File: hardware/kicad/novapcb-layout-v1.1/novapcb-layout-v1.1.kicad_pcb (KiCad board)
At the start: 6 copper layers, 90 x 70 mm, 129 parts, among them J1 USB-C_2.0, J10 CRSF_solder_pad, J11 ESC_solder_pad, J12 ESC_solder_pad, J13 ESC_solder_pad, J14 ESC_solder_pad, J15 ESC_solder_pad, J16 ESC_solder_pad, J17 ESC_solder_pad, J18 ESC_solder_pad, J19 MAUCH2_6P, J2 microSD_DM3AT, J20 CAN_4P, J3 TELEM_6P, J4 MAUCH_6P, J5 GPS_MAG_10P, J9 SWD_10P, Q2 AO3401A, Q3 AO4262E, Q4 AO4262E, Q5 AO3400A, U1 STM32H743VITx, U11 LM74700-Q1, U12 LM74700-Q1, U13 LP5907MFX-3.3, U14 TJA1051TK/3, U15 PESD2CAN, U2 AP2112K-3.3, U3 ICM-42688-P_LGA-14_2.5x3mm_P0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, U4 DPS310, U5 USBLC6-2P6, U6 TPS25940A, U7 LPS22HB, U8 BMI088, U9 LSM6DSV16X, Y1 8MHz

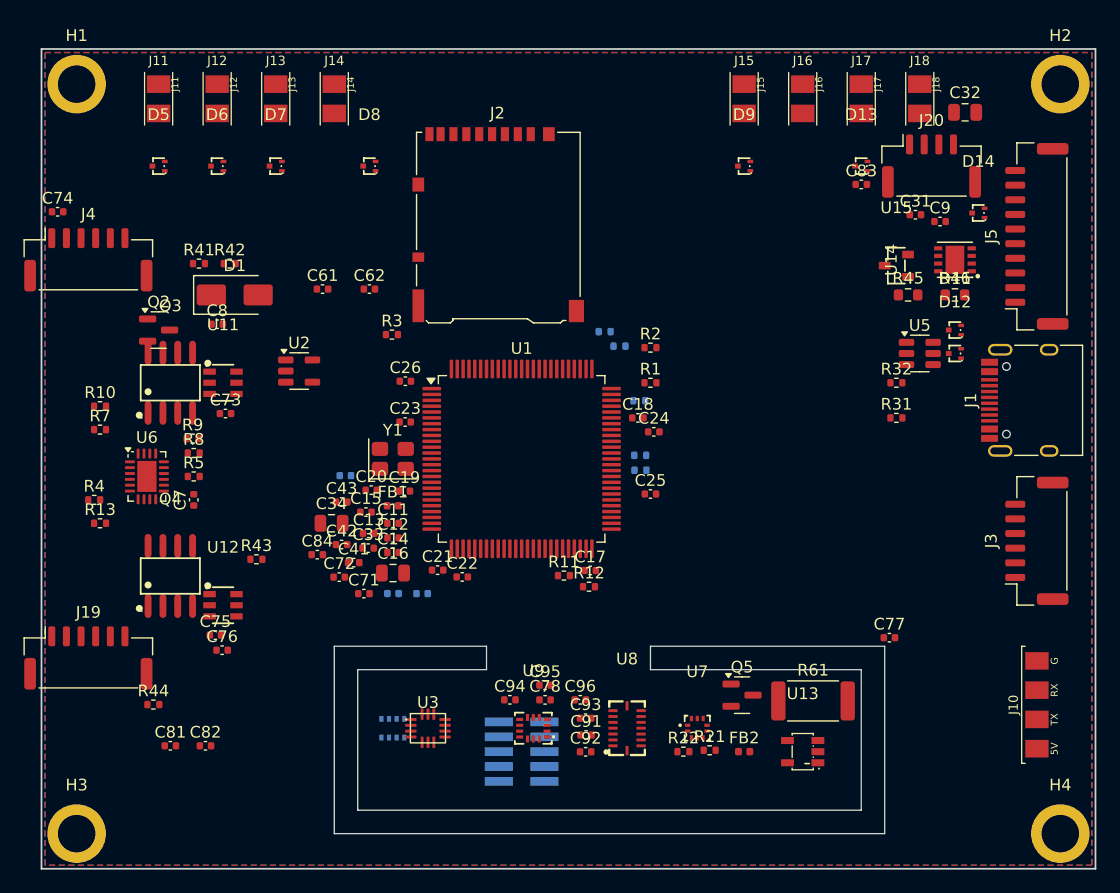
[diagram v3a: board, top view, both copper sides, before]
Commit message: hw: R4 Freerouting on valid re-mux v13 — plateau at 37 unrouted (77% routed)
Master's gate: ~100% completion required. Result: 77% (plateau at
36-37 unrouted across passes 11-21). BELOW gate; below master's
quoted ~85% original-placement plateau.

Freerouting v2.2.3 -mp 30, 33 min, 21 passes:
  pass  1: 82 unrouted
  pass  6: 44
  pass 10: 40
  pass 11: 36  (lowest)
  pass 21: 37  (final — plateau)

PCB state after SES import: 610 tracks + 54 vias placed.
DRC: 144 unconnected items (was 235 before routing) — 91 connections
made. Net topology: 37 of 159 nets fully unrouted.

Compare to ORIGINAL placement -mp 30: 25 unrouted (84% routed).
The re-placement actually performed WORSE — 12 more nets unrouted.

Likely reasons (honest):
1. Sensor island on S edge forces SPI3 (PB3/4/5 on N) + I2C1 (PB6/7
   on N) to traverse the entire board diagonally. ~6 long traces from
   MCU-N down to S-island = the routing bottleneck.
2. ESC pads on N edge force MOT3/MOT4 (PA0/PA1 on W) + MOT7/MOT8
   (PD12/PD13 on E) to route across the board to N-edge ESC pads.
3. The LQFP-100 pin-mux locked SPI3/I2C1 to N, which conflicts with
   sensor-island-on-S strategy. Master's strategy assumed re-mux
   could fix this; it cannot on this package.

Per master's authorized fallback: stackup layer-rebalance — convert
inner plane layer(s) to signal layers for routing room.

Renders: render_fr_v13_top.png + bot.png

Co-Authored-By: Claude Opus 4.7 <noreply@anthropic.com>
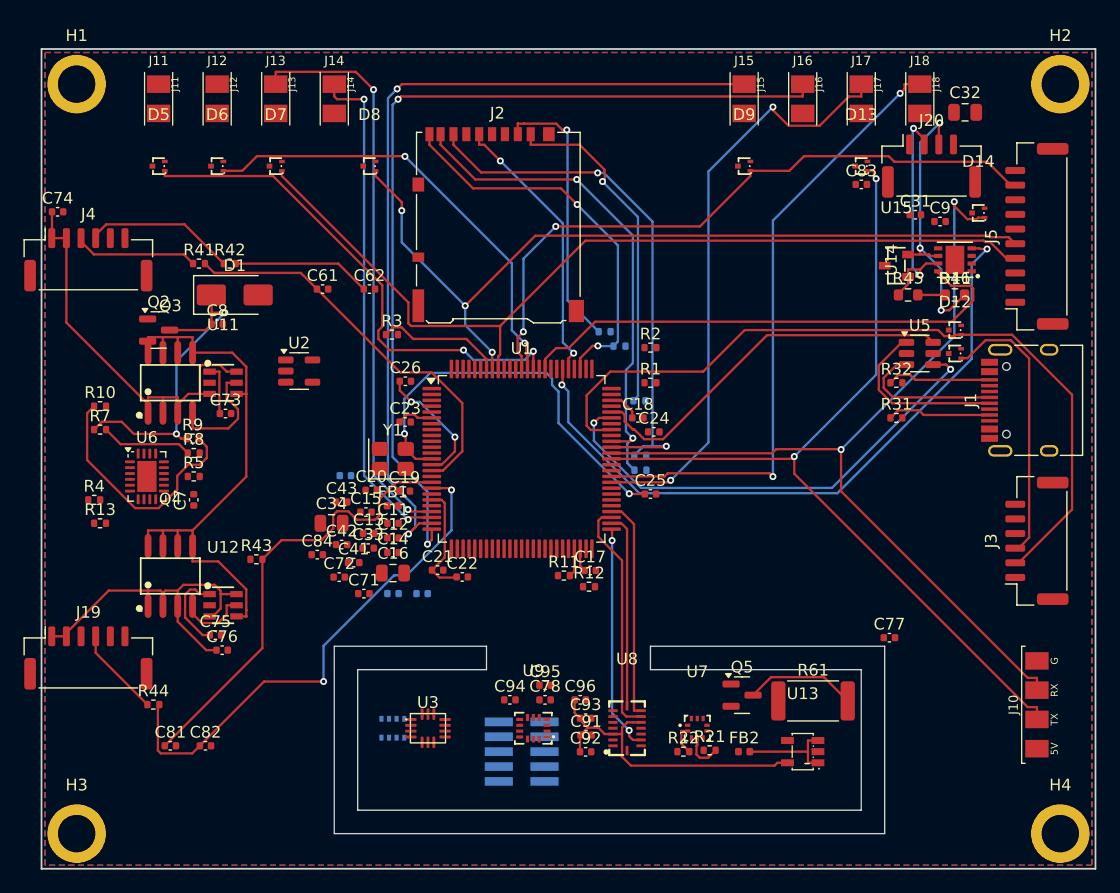
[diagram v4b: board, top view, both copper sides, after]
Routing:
- net I2C1_SCL: track 0.00 -> 79.4 mm
- net MOT6: track 0.00 -> 76.6 mm, vias 0 -> 2
- net USART6_RX: track 0.00 -> 76.4 mm, vias 0 -> 2
- net USART6_TX: track 0.00 -> 75.1 mm, vias 0 -> 2
- net I2C1_SDA: track 0.00 -> 74.2 mm, vias 0 -> 3
- net MOT5: track 0.00 -> 71.7 mm, vias 0 -> 2
- net USART1_TX: track 0.00 -> 67.6 mm
- net CAN1_RX: track 0.00 -> 57.8 mm, vias 0 -> 2
- net BUZZER: track 0.00 -> 56.7 mm, vias 0 -> 2
- net MOT8: track 0.00 -> 53.5 mm, vias 0 -> 2
- net MOT7: track 0.00 -> 51.1 mm, vias 0 -> 2
- net +5V_BEC: track 0.00 -> 51.0 mm
- net MOT3: track 0.00 -> 49.2 mm, vias 0 -> 2
- net SDMMC1_D0: track 0.00 -> 47.6 mm, vias 0 -> 2
- net GPIO_CAN1_SILENT: track 0.00 -> 44.2 mm
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
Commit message: hw: R4 stackup layer-rebalance — L4 becomes signal (master 2026-05-22)
Master's authorized fallback after re-placement plateau (77% < gate).

Stackup change (KEEP same 6-layer JLC06161H-7628 fab — only L4 copper
role changes):
  OLD: L1 Sig / L2 GND / L3 +3V3 / L4 +5V / L5 GND / L6 Sig (2 sig)
  NEW: L1 Sig / L2 GND / L3 +3V3 / L4 SIGNAL / L5 GND / L6 Sig (3 sig)

+50% routing room. Every signal layer adjacent to a reference plane
(L1→L2, L4→L3/L5, L6→L5). No adjacent-signal crosstalk.

Applied:
- layer_rebalance.py: removed 2 +5V zones from In3.Cu, stripped routes
- USB pair impedance recompute on new stackup (IMPEDANCE_RECOMPUTE_L4.md):
  - L1 + L6: W=0.30/S=0.10 (unchanged) → Z_diff = 94.4Ω ✓
  - L4: W=0.16/S=0.10 → Z_diff ≈ 87Ω ✓ (within USB ±15%)
  - Decision: USB pair stays L1/L6 to avoid via geometry discontinuity;
    L4 for all OTHER signals (~150 nets, the bottleneck)
- run_3layer.py: Freerouting now keeps In3.Cu as signal layer, strips
  In1/In2/In4 + plane nets (only GND + +3V3 remain as planes; +5V is
  now a routed signal).

PCB unchanged geometrically: placement v13, slot, smalls — all kept.
ONLY L4's copper role changes.

Freerouting v2.2.3 -mp 30 running on 3-signal stackup.

Co-Authored-By: Claude Opus 4.7 <noreply@anthropic.com>
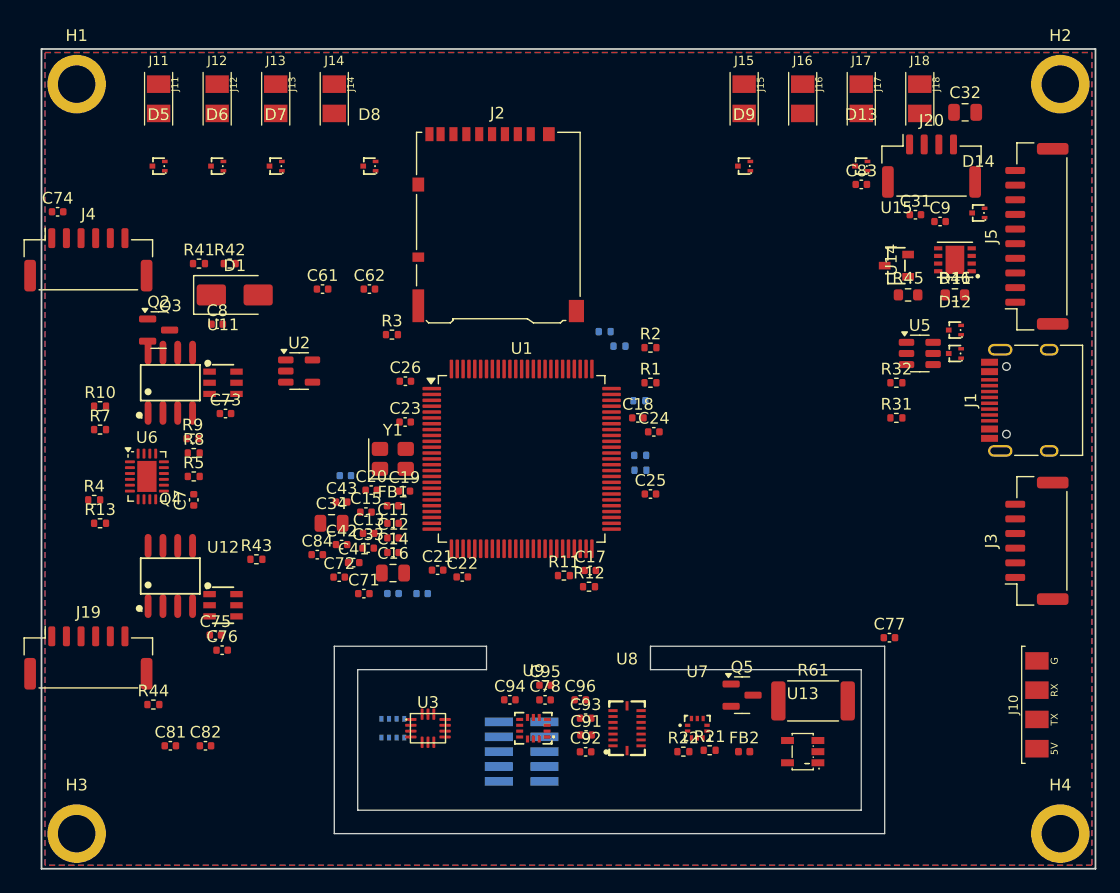
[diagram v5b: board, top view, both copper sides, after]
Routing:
- net I2C1_SCL: track 79.4 -> 0.00 mm
- net MOT6: track 76.6 -> 0.00 mm, vias 2 -> 0
- net USART6_RX: track 76.4 -> 0.00 mm, vias 2 -> 0
- net USART6_TX: track 75.1 -> 0.00 mm, vias 2 -> 0
- net I2C1_SDA: track 74.2 -> 0.00 mm, vias 3 -> 0
- net MOT5: track 71.7 -> 0.00 mm, vias 2 -> 0
- net USART1_TX: track 67.6 -> 0.00 mm
- net CAN1_RX: track 57.8 -> 0.00 mm, vias 2 -> 0
- net BUZZER: track 56.7 -> 0.00 mm, vias 2 -> 0
- net MOT8: track 53.5 -> 0.00 mm, vias 2 -> 0
- net MOT7: track 51.1 -> 0.00 mm, vias 2 -> 0
- net +5V_BEC: track 51.0 -> 0.00 mm
- net MOT3: track 49.2 -> 0.00 mm, vias 2 -> 0
- net SDMMC1_D0: track 47.6 -> 0.00 mm, vias 2 -> 0
- net GPIO_CAN1_SILENT: track 44.2 -> 0.00 mm
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- removed copper zone on In3.Cu, net +5V

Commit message: hw: R4 3-layer Freerouting — 88.8% routed (20 unrouted), SES applied
3-signal stackup (L1/L4/L6) + v13 placement + valid re-mux:
- Java FR completed naturally at -mp 30 in 2h 2min (pass 26 plateau)
- 179 nets total → 20 unrouted → 159 routed = **88.8%**
- Improved from 2-signal result: 25 (84%) → 20 (88.8%) = +4.8 pts
- SES on disk (76 KB), imported successfully

Process note: pre-empted my Python wrapper's 2h TIMEOUT by SIGKILL'ing
the wrapper (PID 1685284) at 53min mark, orphaning Java FR (1685298)
to init. Java continued unimpeded, completed naturally, wrote SES.
Master's reinforced lesson applied: timeouts are safety nets, never
guillotines on converging runs.

PCB state: 988 tracks + 113 vias
DRC: 0 shorts, 3 minor copper_edge_clearance (0.21-0.23mm vs 0.30
required); 112 unconnected items (= 20 unrouted nets)

Unrouted residual (15 net names):
  BATT_CURRENT_SENS, GND (one segment), IMU3_CS, IMU3_INT1, MOT1,
  MOT2, NRST, SPI1_MISO/MOSI/SCK, SPI3_MISO/MOSI/SCK, SWCLK, SWDIO

Most are island↔MCU long traces (SPI1, SPI3, IMU3) confirming the
LQFP-100 pin-mux constraint flagged earlier.

+5V WIDTH ISSUE: all 108 +5V track segments are 0.20mm (Default
netclass). Per master's 3A spec, +5V needs ≥1.5-1.8mm trace OR pour
on signal layer. Pending fix.

Per master's directive on meaningful residual: STOP for master's
call. Options: 4-signal fallback (convert L3 too), finishing pass
on the 15 residual nets, or accept and route 15 manually.

Co-Authored-By: Claude Opus 4.7 <noreply@anthropic.com>
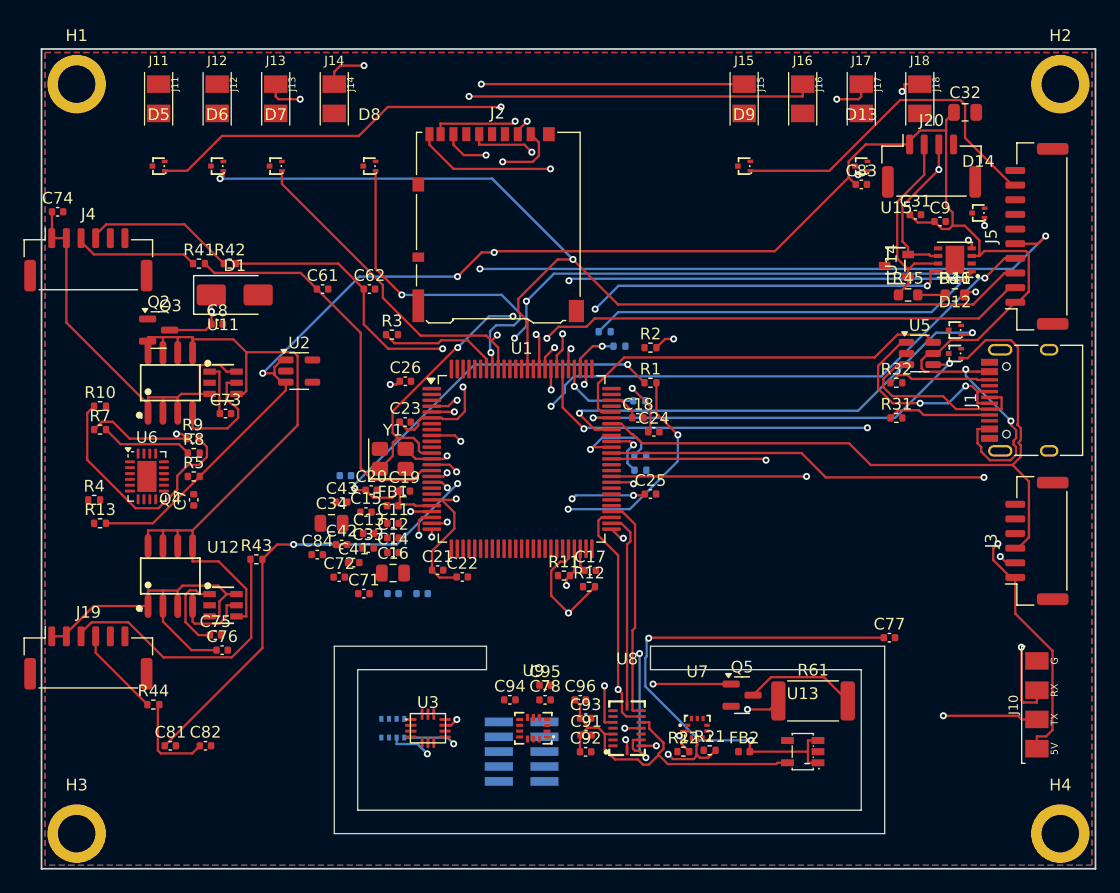
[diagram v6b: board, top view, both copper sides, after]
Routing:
- net +5V: track 0.00 -> 243.0 mm, vias 0 -> 7
- net I2C1_SDA: track 0.00 -> 135.8 mm, vias 0 -> 5
- net I2C1_SCL: track 0.00 -> 117.9 mm, vias 0 -> 4
- net SDMMC1_CMD: track 0.00 -> 99.2 mm, vias 0 -> 4
- net GPS1_TX: track 0.00 -> 94.1 mm, vias 0 -> 2
- net GPS1_RX: track 0.00 -> 86.7 mm, vias 0 -> 2
- net USART6_RX: track 0.00 -> 84.9 mm, vias 0 -> 3
- net USART6_TX: track 0.00 -> 78.6 mm, vias 0 -> 3
- net IMU2_GYR_CS: track 0.00 -> 76.7 mm, vias 0 -> 2
- net MOT6: track 0.00 -> 69.3 mm, vias 0 -> 2
- net VBAT: track 0.00 -> 64.5 mm, vias 0 -> 2
- net MOT5: track 0.00 -> 63.3 mm, vias 0 -> 2
- net USART1_TX: track 0.00 -> 62.4 mm, vias 0 -> 3
- net +5V_BEC: track 0.00 -> 61.7 mm
- net USART1_RX: track 0.00 -> 60.4 mm
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
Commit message: hw: R4 plane-stitch on clean FR3 baseline — 67→30 unconnected
Per master 2026-05-22: do plane stitches NOW on clean FR3 baseline
(commit 14a2d46) — mechanical, headless-doable, needed regardless of
the 12 signal residuals.

Step 1: run_stitch_plane_nets.py
- 176 pads stitched ✓ (vs 170 on tangled board — clean is better)
- 8 skipped (TH) + 1 already-via
- 15 failed (dense MCU/USB areas)

Step 2: fix_mcu_power.py (MCU power pin → decap trace approach)
- 8 GND traces added: U12.2, U9.6, U8.4/6/7, U1.10/19/26 → nearest decap

Net effect: unconnected 67 → 30, DRC 0 → 59 (clashes introduced by stitches+traces)

Remaining 30 unconnected breakdown:
- 12 signal residuals (HELD per master directive — untouched)
- 18 plane items still need stitching/connection:
  - +3V3_IMU: 9 items (C78/C94/C95, U9.5/8) — NOT plane-stitch; needs
    routing from FB2 ferrite output to consumers (separate net)
  - +3V3: 6 items (U1.11/50/75 power pins + a few others — dense MCU
    region where stitch+decap-trace both failed)
  - GND: U1.74, U1.50 (dense MCU power pins)
  - Plus pads on signal-net residuals (U1.86=GPS1_TX appears here
    because the route never reached the pad — it's a signal residual
    in disguise)

Per master "if a handful cannot stitch, flag them — do not force":
The 18 remaining items are the genuine "handful that cannot stitch
in the dense MCU power-pin region". Flagged in residuals JSON.

12 signal residuals UNTOUCHED per directive.

Co-Authored-By: Claude Opus 4.7 <noreply@anthropic.com>
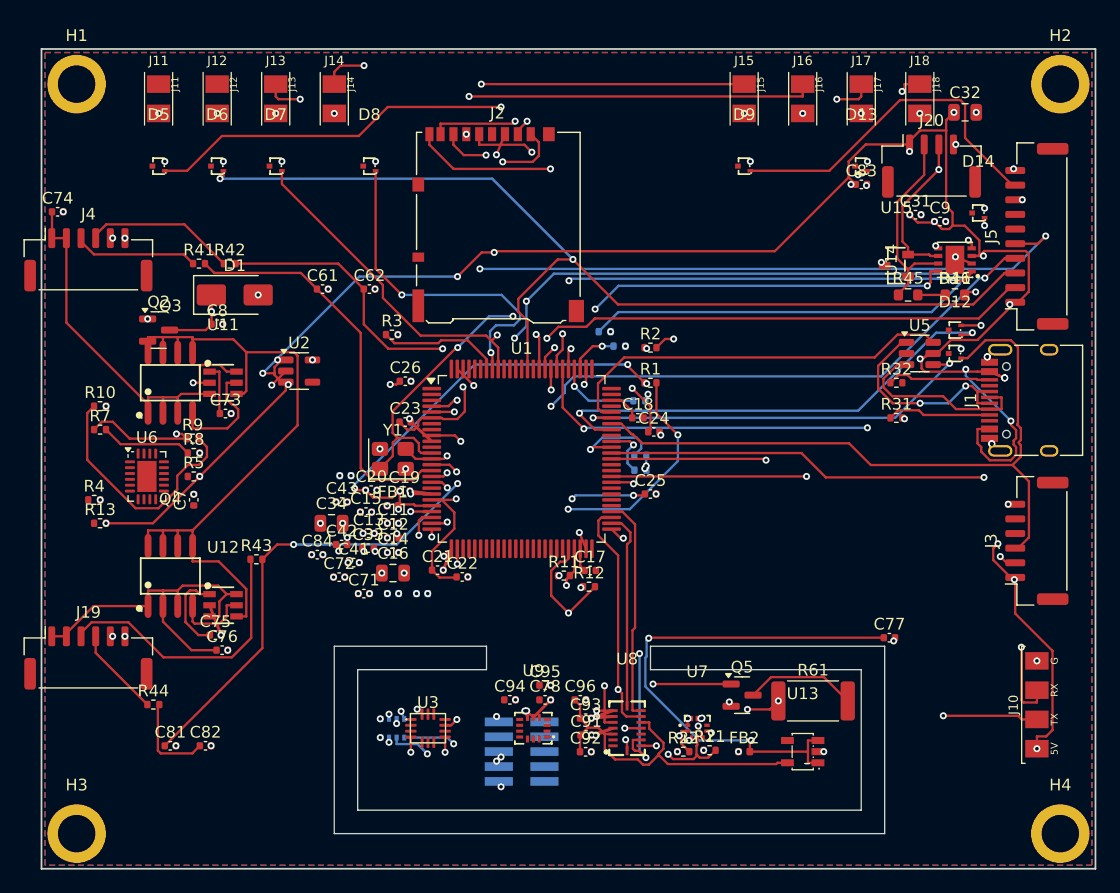
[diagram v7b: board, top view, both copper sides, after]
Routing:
- net GND: track 0.00 -> 50.0 mm, vias 0 -> 113
- net +3V3: track 0.00 -> 9.90 mm, vias 0 -> 42
- net +5V: track 243.0 -> 250.7 mm, vias 7 -> 24
- net +3V3A: track 38.5 -> 39.1 mm, vias 2 -> 6
